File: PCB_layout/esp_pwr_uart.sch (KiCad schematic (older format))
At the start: 38 parts, among them CN7 24VDC, CN8 USB_micro, P1 USB-C_breakout, Q2 DDC114TU, U3 B2405S-2WR2, U4 LM1117-33, U5 CP2102N-A01-GQFN28, U6 24V_BUCK

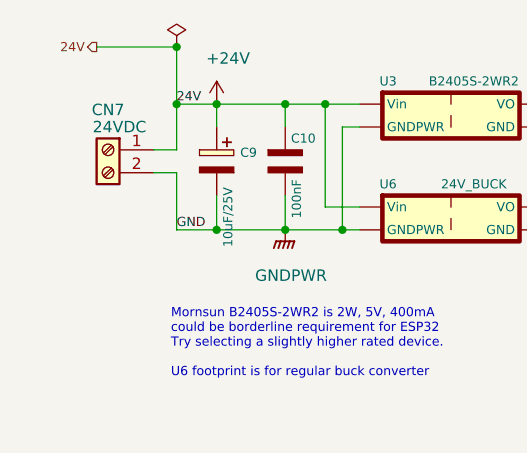
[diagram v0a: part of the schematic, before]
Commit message: added optocoupler for isolation
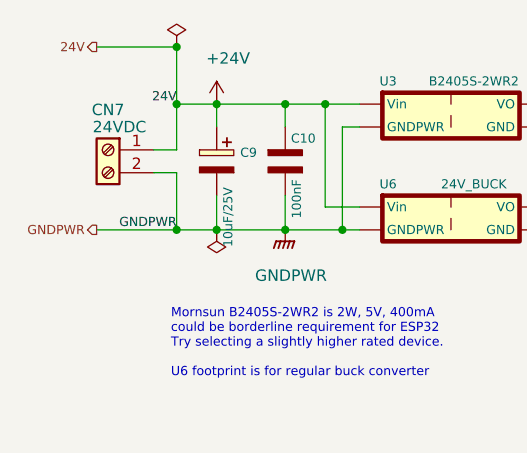
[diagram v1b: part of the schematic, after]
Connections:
- net GND: no longer C10.2 (-), C9.2 (-), CN7.2 (Pin_2), U3.GNDPWR, U6.GNDPWR
- new net GNDPWR: C10.2 (-), C9.2 (-), CN7.2 (Pin_2), U3.GNDPWR, U6.GNDPWR
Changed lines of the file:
@@
 U 1 1 6173F60B
 P 2450 950
+AR Path="/6173F60B" Ref="U3"  Part="1"
+AR Path="/5A452227/6173F60B" Ref="U3"  Part="1"
 F 0 "U3" H 2175 1100 40  0000 C CNN
 F 1 "B2405S-2WR2" H 2550 1100 40  0000 C CNN
@@
 	1    0    0    -1
 $EndComp
-Text Label 1250 900  0    40   ~ 0
+Text Label 1250 900  2    40   ~ 0
 24V
 Text Label 3225 900  0    40   ~ 0
 5V
-Text Label 1250 1450 0    40   ~ 0
-GND
+Text Label 1250 1450 2    40   ~ 0
+GNDPWR
 Text Notes 1225 2100 0    40   ~ 0
 Mornsun B2405S-2WR2 is 2W, 5V, 400mA\ncould be borderline requirement for ESP32\nTry selecting a slightly higher rated device.\n\nU6 footprint is for regular buck converter
@@
 U 1 1 617133F7
 P 2450 1400
+AR Path="/617133F7" Ref="U6"  Part="1"
+AR Path="/5A452227/617133F7" Ref="U6"  Part="1"
 F 0 "U6" H 2175 1550 40  0000 C CNN
 F 1 "24V_BUCK" H 2550 1550 40  0000 C CNN
@@
 Wire Wire Line
 	3025 900  3300 900
+Wire Wire Line
+	1250 1450 900  1450
+Connection ~ 1250 1450
+Text HLabel 900  1450 0    40   Output ~ 0
+GNDPWR
+$Comp
+L power:PWR_FLAG #FLG0102
+U 1 1 616FD3E1
+P 1425 1450
+F 0 "#FLG0102" H 1425 1525 50  0001 C CNN
+F 1 "PWR_FLAG" H 1425 1650 50  0001 C CNN
+F 2 "" H 1425 1450 50  0001 C CNN
+F 3 "~" H 1425 1450 50  0001 C CNN
+	1    1425 1450
+	-1   0    0    1
+$EndComp
 $EndSCHEMATC

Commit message: PCB layout, WIP
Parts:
- added U11: DC_DC_buck_6W, AA_vayu:DC_DC_conv_6W, symbol AA_vayuO2_symbols:DC_DC_buck_6W
- U3: symbol AA_vayuO2_symbols:DC_DC_buck -> AA_vayuO2_symbols:DC_DC_buck_2W
- U6: footprint AA_vayu:DC_DC_buck_LM2596 -> AA_vayu:DC_DC_buck_LM2596_Vertical
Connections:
- net +24V: now also U11.VIN (Vin)
- net 5V: now also U11.VO
- net GND: now also U11.GND
- net GNDPWR: now also U11.GNDPWR
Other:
- note added: "Mornsun B2405S-2WR2 is 2W, 5V, 400mA\ncould be borderline requirement for ESP32\nTry selecting a slightly higher rated device.\n\nU6 footprint is for regular non-isolated buck converter.\nTo save PCB space, mount this vertically using\nan L bracket and use mounting holes. Hook it\nup using wires to U3 pads"
- note removed: "Mornsun B2405S-2WR2 is 2W, 5V, 400mA\ncould be borderline requirement for ESP32\nTry selecting a slightly higher rated device.\n\nU6 footprint is for regular buck converter"
- moved on the sheet: C10, C11, C9, CN7, U3, U6

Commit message: BOM, WIP
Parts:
- C12, C17, C9: footprint AA_vayu:CP_Elec_6.3x5.4 -> AA_vayu:CP_Elec_6.3x7.7
- C13: footprint AA_vayu:CP_Elec_6.3x5.3 -> AA_vayu:CP_Elec_6.3x7.7
- Q2: value DDC114TU -> DTC123YCA
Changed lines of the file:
@@
 F 0 "C12" H 4678 1588 40  0000 L CNN
 F 1 "10uF/25V" V 4625 1175 40  0000 L CNN
-F 2 "AA_vayu:CP_Elec_6.3x5.4" H 4575 1550 60  0001 C CNN
+F 2 "AA_vayu:CP_Elec_6.3x7.7" H 4575 1550 60  0001 C CNN
 F 3 "" H 4575 1550 60  0000 C CNN
 	1    4575 1550
@@
 F 0 "C13" H 5628 1588 40  0000 L CNN
 F 1 "22uF/25V" V 5575 1175 40  0000 L CNN
-F 2 "AA_vayu:CP_Elec_6.3x5.3" H 5525 1550 60  0001 C CNN
+F 2 "AA_vayu:CP_Elec_6.3x7.7" H 5525 1550 60  0001 C CNN
 F 3 "" H 5525 1550 60  0000 C CNN
 	1    5525 1550
@@
 F 0 "C17" H 3050 5625 40  0000 L CNN
 F 1 "10uF/25V" V 3075 5100 40  0000 L CNN
-F 2 "AA_vayu:CP_Elec_6.3x5.4" H 3025 5475 60  0001 C CNN
+F 2 "AA_vayu:CP_Elec_6.3x7.7" H 3025 5475 60  0001 C CNN
 F 3 "" H 3025 5475 60  0000 C CNN
 	1    3025 5475
@@
 P 7875 1350
 F 0 "Q2" H 8071 1395 50  0000 L CNN
-F 1 "DDC114TU" H 8071 1305 50  0000 L CNN
+F 1 "DTC123YCA" H 8071 1305 50  0000 L CNN
 F 2 "AA_vayu:SOT-363_SC-70-6" H 8075 1450 50  0001 C CNN
 F 3 "https://www.diodes.com/assets/Datasheets/ds30345.pdf" H 7875 1350 50  0001 C CNN
@@
 P 7875 2250
 F 0 "Q2" H 8071 2205 50  0000 L CNN
-F 1 "DDC114TU" H 8071 2295 50  0000 L CNN
+F 1 "DTC123YCA" H 8071 2295 50  0000 L CNN
 F 2 "AA_vayu:SOT-363_SC-70-6" H 8075 2350 50  0001 C CNN
 F 3 "https://www.diodes.com/assets/Datasheets/ds30345.pdf" H 7875 2250 50  0001 C CNN
@@
 F 0 "C9" H 1528 1538 40  0000 L CNN
 F 1 "10uF/25V" V 1475 1125 40  0000 L CNN
-F 2 "AA_vayu:CP_Elec_6.3x5.4" H 1425 1500 60  0001 C CNN
+F 2 "AA_vayu:CP_Elec_6.3x7.7" H 1425 1500 60  0001 C CNN
 F 3 "" H 1425 1500 60  0000 C CNN
 	1    1425 1500

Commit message: final production files generated
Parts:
- C19: footprint AA_vayu:CP_Elec_6.3x5.4 -> AA_vayu:CP_Elec_6.3x7.7
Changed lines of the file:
@@
 F 0 "C19" H 3500 5625 40  0000 L CNN
 F 1 "10uF/25V" V 3525 5100 40  0000 L CNN
-F 2 "AA_vayu:CP_Elec_6.3x5.4" H 3475 5475 60  0001 C CNN
+F 2 "AA_vayu:CP_Elec_6.3x7.7" H 3475 5475 60  0001 C CNN
 F 3 "" H 3475 5475 60  0000 C CNN
 	1    3475 5475
